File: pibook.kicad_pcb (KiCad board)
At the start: 2 copper layers, 85 x 85 mm, 83 parts, among them IC1 ATTINY48-A, J1 ComputeModule, J2 TRS_JACK_3PIN, P1 CONN_01X40, P2 USB_OTG, P3 CONN_01X02, P4 CONN_02X05, P5 USB_A, P6 CONN_02X06, Q1 Si2323DS, Q2 Si2323DS, Q3 BSS138P, Q4 Si2323DS, SW91 SPST, U1 FAN5333, U2 BQ21040, U3 NCP1532

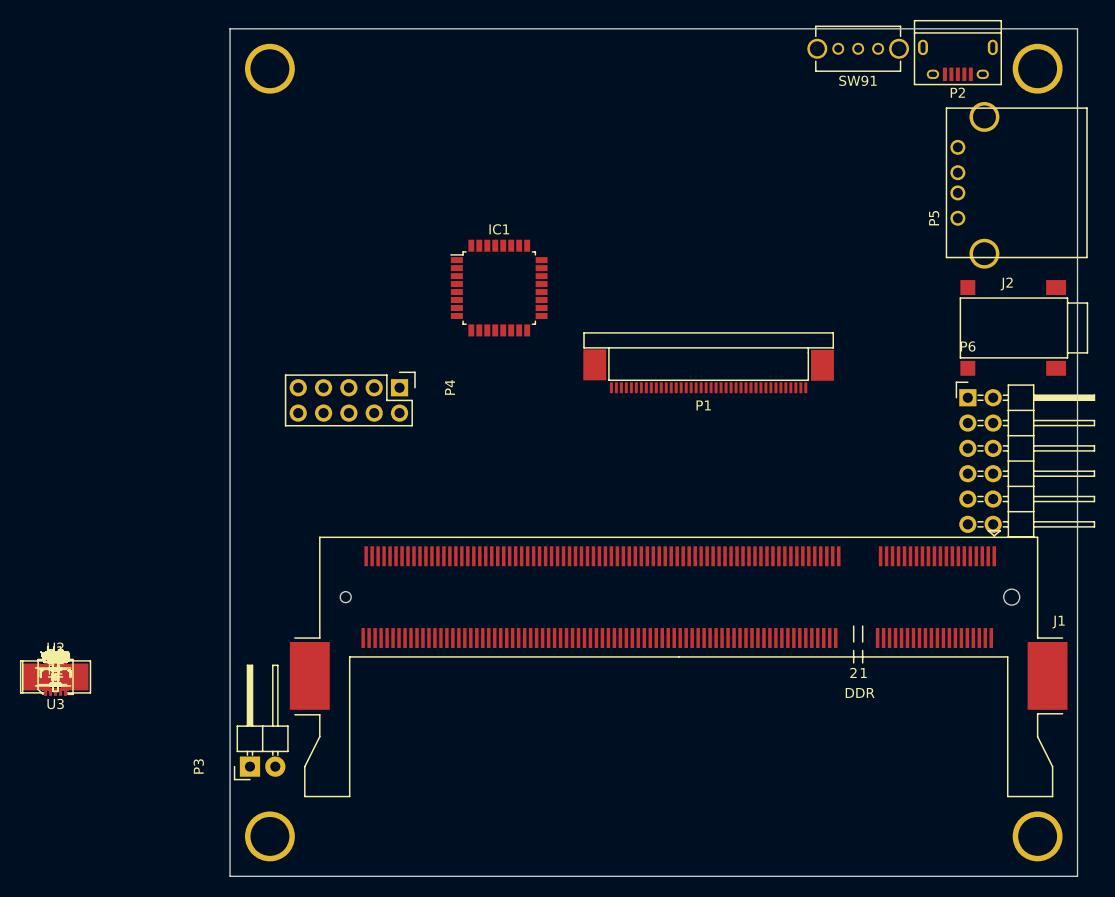
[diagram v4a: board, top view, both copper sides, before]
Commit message: Some more component placement
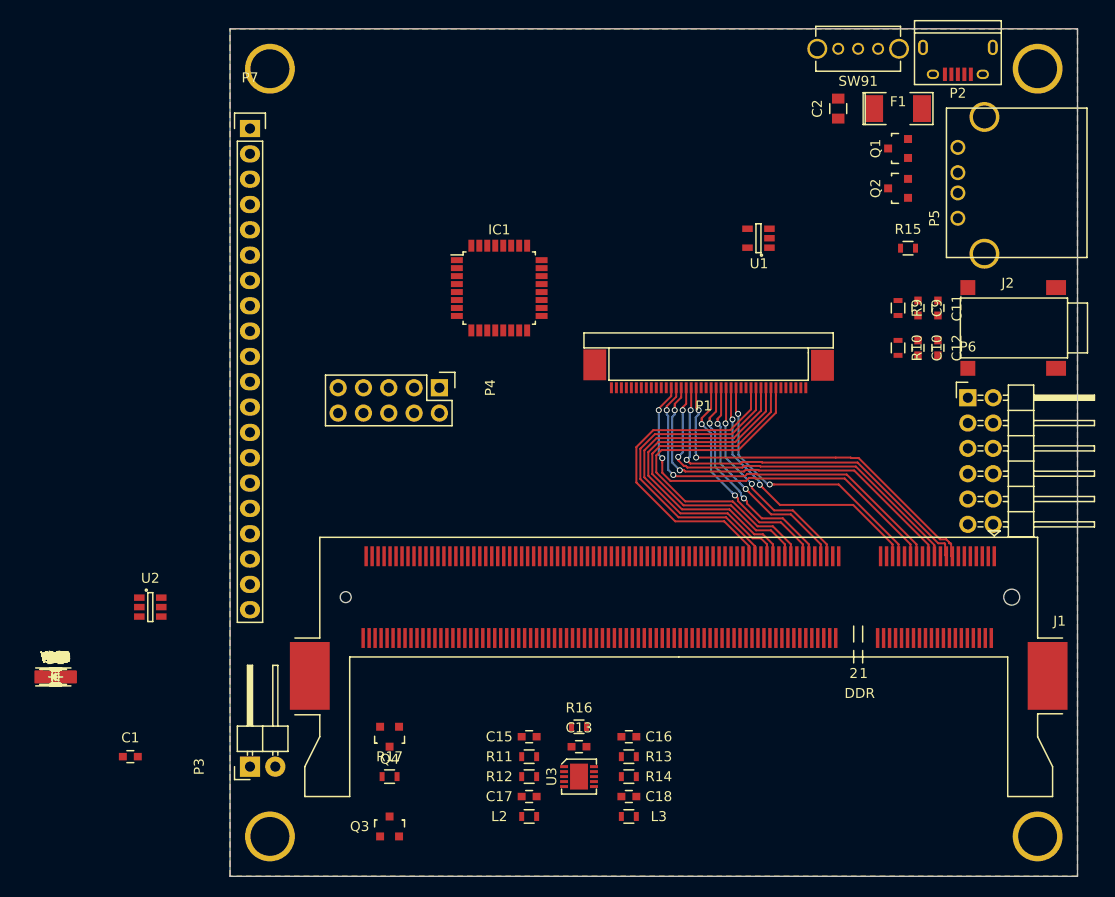
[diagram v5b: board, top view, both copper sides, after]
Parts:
- added P7: CONN_01X20, Pin_Headers:Pin_Header_Straight_1x20, F.Cu at (75.0, 118.0)
- moved F1 101.9 mm to (140.0, 116.0)
- moved Q1 99.7 mm to (140.0, 120.0), turned to 90 degrees
- moved Q2 97.7 mm to (140.0, 124.0), turned to 90 degrees
- moved C2 97.0 mm to (134.0, 116.0), turned to 90 degrees
- moved C11 95.9 mm to (144.0, 136.0), turned to 270 degrees
- moved R15 95.7 mm to (141.0, 130.0)
- moved C12 94.5 mm to (144.0, 140.0), turned to 270 degrees
- moved C9 94.1 mm to (142.0, 136.0), turned to 270 degrees
- moved C10 92.6 mm to (142.0, 140.0), turned to 270 degrees
- moved R9 92.2 mm to (140.0, 136.0), turned to 270 degrees
- moved R10 90.7 mm to (140.0, 140.0), turned to 270 degrees
- moved U1 83.1 mm to (126.0, 129.0), turned to 180 degrees
- moved L3 59.2 mm to (113.0, 187.0)
- moved C18 58.7 mm to (113.0, 185.0), turned to 180 degrees
- moved R14 58.4 mm to (113.0, 183.0)
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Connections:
- IC1 pad 1: (no net) -> /KEY_C3
- IC1 pad 10: (no net) -> /KEY_C6
- IC1 pad 11: (no net) -> /KEY_C7
- IC1 pad 12: (no net) -> /KEY_R1
- IC1 pad 2: (no net) -> /KEY_C4
- IC1 pad 23: (no net) -> /KEY_C8
- IC1 pad 24: (no net) -> /KEY_C9
- IC1 pad 25: (no net) -> /KEY_C10
- IC1 pad 26: (no net) -> /KEY_C11
- IC1 pad 27: (no net) -> /KEY_R0
- IC1 pad 3: (no net) -> /KEY_R4
- IC1 pad 30: (no net) -> /KEY_C0
- IC1 pad 31: (no net) -> /KEY_C1
- IC1 pad 32: (no net) -> /KEY_C2
- IC1 pad 6: (no net) -> /KEY_R5
- IC1 pad 7: (no net) -> /KEY_R2
- IC1 pad 8: (no net) -> /KEY_R3
- IC1 pad 9: (no net) -> /KEY_C5
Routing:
- net /LCD_B_7: track 0.00 -> 38.5 mm, vias 0 -> 2
- net /LCD_B_5: track 0.00 -> 38.3 mm, vias 0 -> 2
- net /LCD_B_3: track 0.00 -> 38.3 mm, vias 0 -> 2
- net /LCD_B_6: track 0.00 -> 38.1 mm, vias 0 -> 2
- net /LCD_B_4: track 0.00 -> 38.1 mm, vias 0 -> 2
- net /LCD_B_2: track 0.00 -> 37.8 mm, vias 0 -> 2
- net /LCD_R_2: track 0.00 -> 35.7 mm
- net /LCD_R_3: track 0.00 -> 35.5 mm
- net /LCD_R_4: track 0.00 -> 34.8 mm
- net /LCD_R_5: track 0.00 -> 34.6 mm
- net /LCD_R_6: track 0.00 -> 33.8 mm
- net /LCD_R_7: track 0.00 -> 33.7 mm
- net /LCD_G_2: track 0.00 -> 28.0 mm, vias 0 -> 2
- net /LCD_G_3: track 0.00 -> 27.9 mm, vias 0 -> 2
- net /LCD_G_7: track 0.00 -> 22.8 mm, vias 0 -> 2
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- added copper zone on B.Cu, net GND
- added copper zone on F.Cu, net GND
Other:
- net class Default: trace_width 0.25 -> 0.2

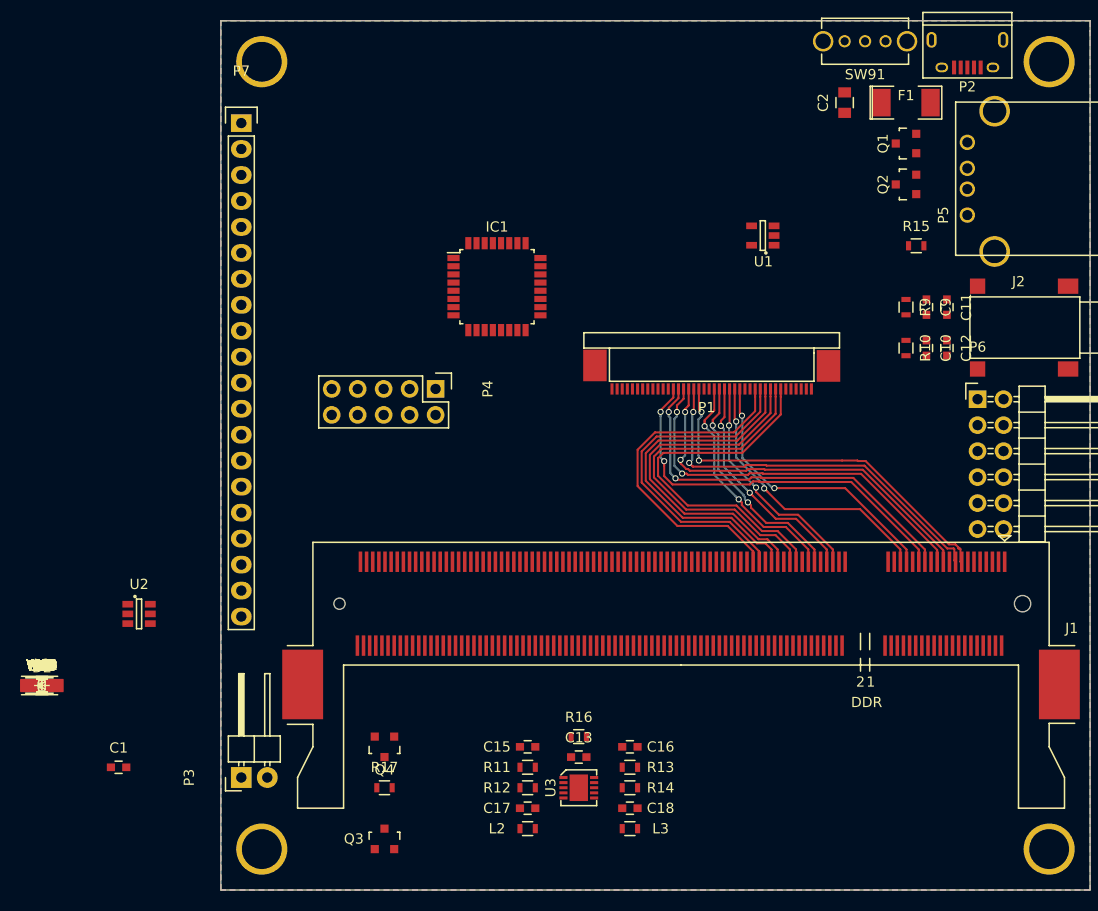
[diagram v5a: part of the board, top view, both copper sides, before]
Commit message: All components placed
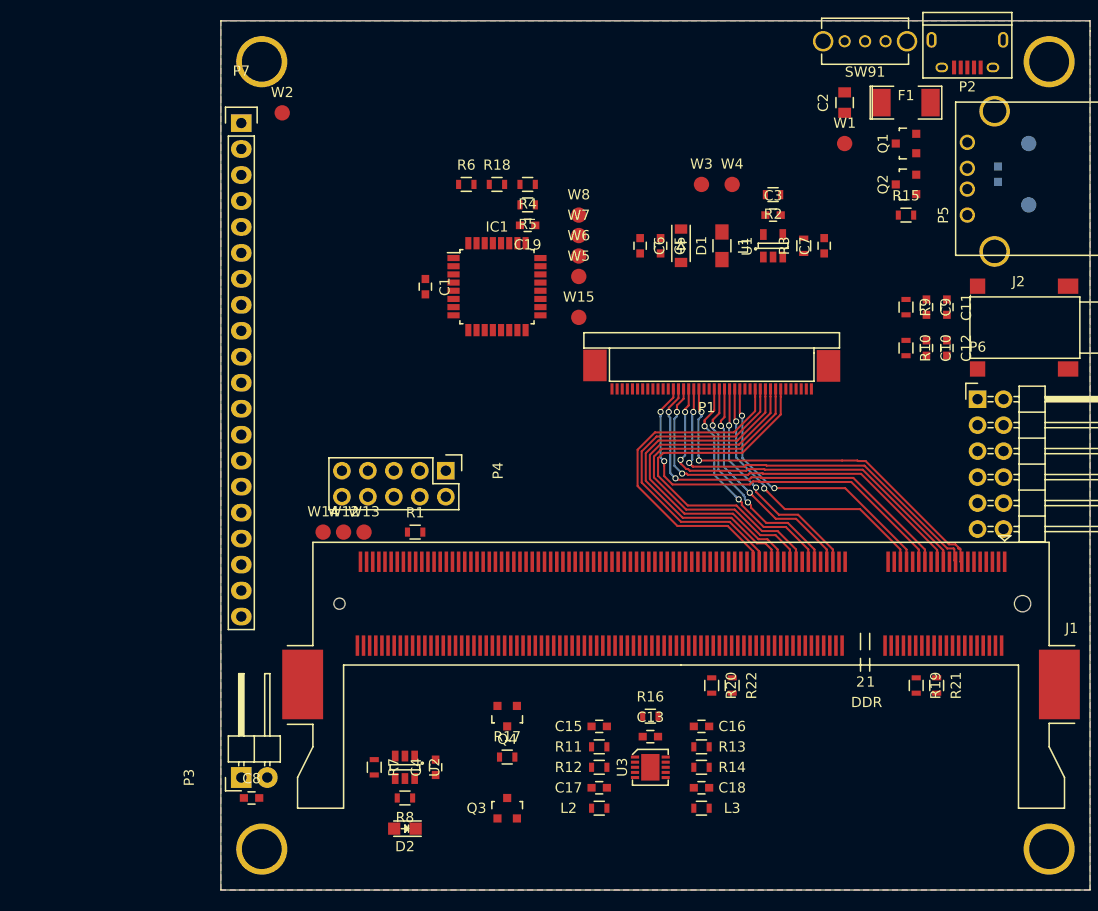
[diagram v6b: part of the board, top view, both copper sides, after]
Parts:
- removed W9: VBAT, Measurement_Points:Measurement_Point_Round-SMD-Pad_Small
- C14, W10, W11: moved to B.Cu
- moved W10 110.1 mm to (152.0, 120.0)
- moved W11 107.3 mm to (152.0, 126.0)
- moved C14 106.0 mm to (149.0, 123.0), turned to 90 degrees
- moved W1 94.7 mm to (134.0, 120.0)
- moved C7 87.8 mm to (132.0, 130.0), turned to 90 degrees
- moved R21 87.5 mm to (143.0, 173.0), turned to 270 degrees
- moved R2 86.1 mm to (127.0, 125.0), turned to 180 degrees
- moved R3 86.0 mm to (130.0, 130.0), turned to 90 degrees
- moved R19 85.5 mm to (141.0, 173.0), turned to 270 degrees
- moved C3 85.0 mm to (127.0, 127.0)
- moved W4 83.4 mm to (123.0, 124.0)
- moved W3 81.0 mm to (120.0, 124.0)
- moved L1 79.2 mm to (122.0, 130.0), turned to 270 degrees
- moved D1 75.9 mm to (118.0, 130.0), turned to 270 degrees
- moved C5 74.2 mm to (116.0, 130.0), turned to 270 degrees
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
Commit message: Some more power routing
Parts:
- added REF**: VIA_0.6MM, ComputeModule:VIA_0.6MM, F.Cu at (96.0, 149.0)
- added REF**: VIA_0.6MM, ComputeModule:VIA_0.6MM, F.Cu at (157.0, 165.0)
- added REF**: VIA_0.6MM, ComputeModule:VIA_0.6MM, F.Cu at (149.0, 183.0)
- added REF**: VIA_0.6MM, ComputeModule:VIA_0.6MM, F.Cu at (143.0, 189.0)
- added REF**: VIA_0.6MM, ComputeModule:VIA_0.6MM, F.Cu at (86.0, 190.0)
- added REF**: VIA_0.6MM, ComputeModule:VIA_0.6MM, F.Cu at (109.0, 190.0)
- added REF**: VIA_0.6MM, ComputeModule:VIA_0.6MM, F.Cu at (74.0, 186.0)
- added REF**: VIA_0.6MM, ComputeModule:VIA_0.6MM, F.Cu at (80.0, 191.0)
- added REF**: VIA_0.6MM, ComputeModule:VIA_0.6MM, F.Cu at (83.0, 184.0)
- added REF**: VIA_0.6MM, ComputeModule:VIA_0.6MM, F.Cu at (90.0, 178.5)
- added REF**: VIA_0.6MM, ComputeModule:VIA_0.6MM, F.Cu at (106.0, 181.0)
- added REF**: VIA_0.6MM, ComputeModule:VIA_0.6MM, F.Cu at (98.0, 151.0)
- added REF** (x2): VIA_0.6MM, ComputeModule:VIA_0.6MM, F.Cu at (92.8, 178.5)
- added REF**: VIA_0.6MM, ComputeModule:VIA_0.6MM, F.Cu at (115.0, 181.0)
- added REF**: VIA_0.6MM, ComputeModule:VIA_0.6MM, F.Cu at (106.0, 175.0)
- added REF**: VIA_0.6MM, ComputeModule:VIA_0.6MM, F.Cu at (115.0, 182.0)
- added REF**: VIA_0.6MM, ComputeModule:VIA_0.6MM, F.Cu at (115.0, 180.0)
- added REF**: VIA_0.6MM, ComputeModule:VIA_0.6MM, F.Cu at (150.0, 191.0)
- added REF**: VIA_0.6MM, ComputeModule:VIA_0.6MM, F.Cu at (156.0, 185.0)
- added REF**: VIA_0.6MM, ComputeModule:VIA_0.6MM, F.Cu at (98.0, 158.0)
- added REF**: VIA_0.6MM, ComputeModule:VIA_0.6MM, F.Cu at (95.0, 158.0)
- added REF**: VIA_0.6MM, ComputeModule:VIA_0.6MM, F.Cu at (157.0, 118.0)
- added REF**: VIA_0.6MM, ComputeModule:VIA_0.6MM, F.Cu at (157.0, 126.0)
- added REF**: VIA_0.6MM, ComputeModule:VIA_0.6MM, F.Cu at (157.0, 136.0)
- added REF**: VIA_0.6MM, ComputeModule:VIA_0.6MM, F.Cu at (157.0, 144.0)
- added REF**: VIA_0.6MM, ComputeModule:VIA_0.6MM, F.Cu at (157.0, 154.0)
- C14: moved to F.Cu
- moved R16 18.4 mm to (101.0, 188.0)
- moved C1 8.66 mm to (99.2, 140.0), turned to 0 degrees
- moved C14 7.00 mm to (142.0, 123.0)
- moved C13 6.00 mm to (115.0, 184.0)
- moved Q1 2.24 mm to (139.0, 122.0)
- moved R15 2.24 mm to (142.0, 126.0), turned to 90 degrees
- moved C3 2.00 mm to (127.0, 129.0)
- moved C5 2.00 mm to (116.0, 132.0)
- moved C6 2.00 mm to (114.0, 132.0)
- moved C7 2.00 mm to (132.0, 132.0)
- moved D1 2.00 mm to (118.0, 132.0)
- moved L1 2.00 mm to (122.0, 132.0)
- moved R2 2.00 mm to (127.0, 127.0)
- moved R3 2.00 mm to (130.0, 132.0)
- moved U1 2.00 mm to (127.0, 132.0)
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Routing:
- net +BATT: track 0.00 -> 271.4 mm, vias 0 -> 5
- net /PWR_ENABLE: track 0.00 -> 168.5 mm, vias 0 -> 3
- net +VUSB_IN: track 0.00 -> 154.6 mm
- net /USB_D-: track 0.00 -> 82.0 mm
- net /USB_D+: track 0.00 -> 80.9 mm
- net +1V8: track 0.00 -> 59.9 mm
- net +3V3: track 0.00 -> 59.8 mm
- net /LCD_CLK: track 0.00 -> 46.8 mm, vias 0 -> 2
- net /LCD_DEN: track 0.00 -> 46.8 mm, vias 0 -> 2
- net /LCD_VSYNC: track 0.00 -> 42.9 mm, vias 0 -> 2
- net /LCD_HSYNC: track 0.00 -> 41.6 mm, vias 0 -> 2
- net /CM_VBAT: track 0.00 -> 33.7 mm
- net Net-(R8-Pad2): track 0.00 -> 18.0 mm
- net Net-(C16-Pad2): track 0.00 -> 8.20 mm
- net Net-(C15-Pad2): track 0.00 -> 8.20 mm
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
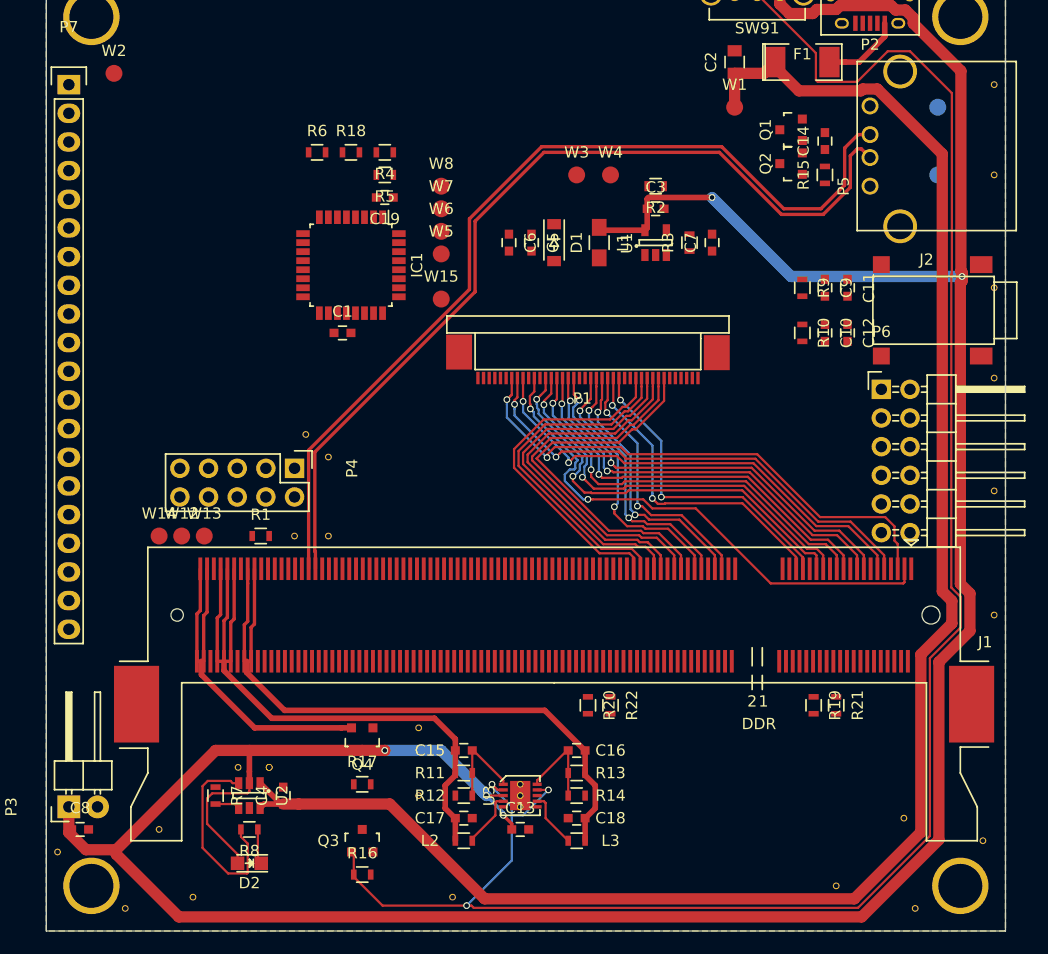
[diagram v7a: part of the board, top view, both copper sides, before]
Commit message: AVR route out mostly done
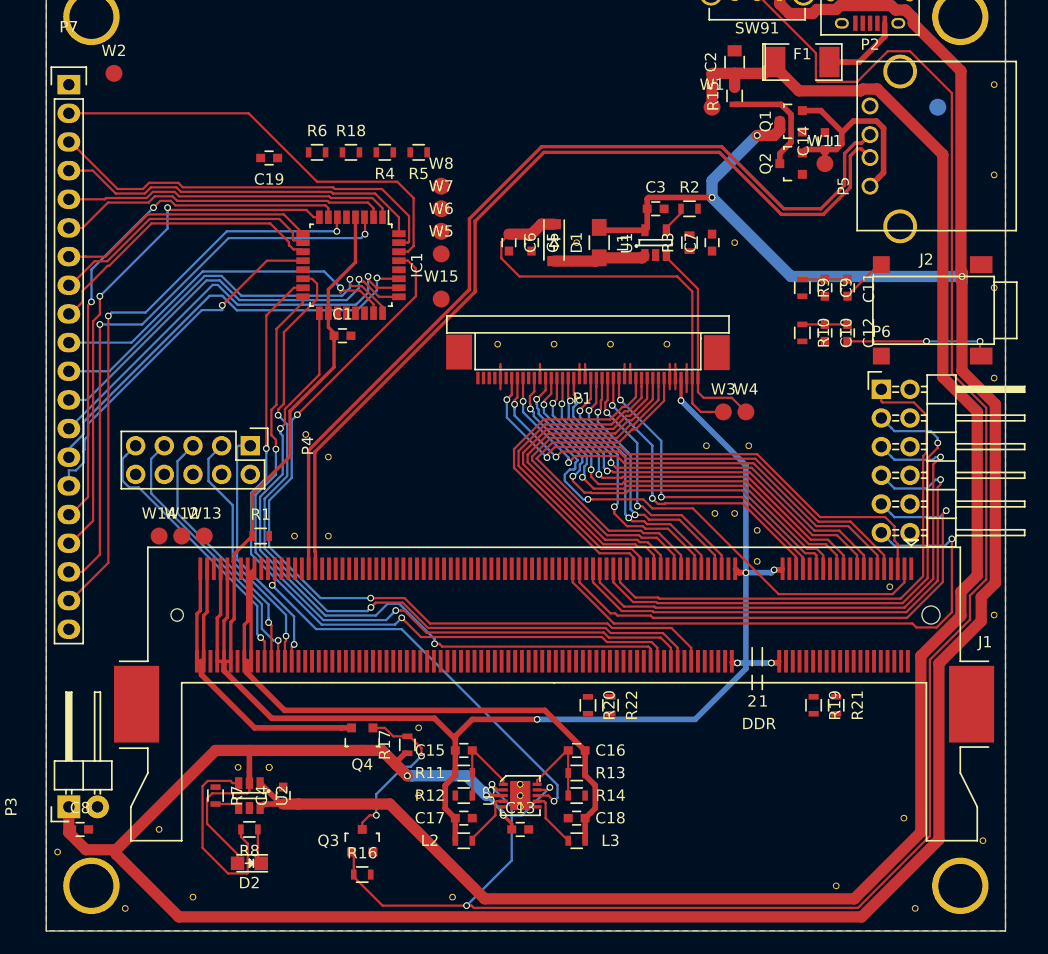
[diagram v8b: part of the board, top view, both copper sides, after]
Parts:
- removed the REF** at (157.0, 154.0)
- added REF**: VIA_0.6MM, ComputeModule:VIA_0.6MM, F.Cu at (136.0, 157.5)
- added REF**: VIA_0.6MM, ComputeModule:VIA_0.6MM, F.Cu at (120.0, 132.0)
- added REF**: VIA_0.6MM, ComputeModule:VIA_0.6MM, F.Cu at (136.0, 160.2)
- added REF**: VIA_0.6MM, ComputeModule:VIA_0.6MM, F.Cu at (132.2, 156.0)
- added REF**: VIA_0.6MM, ComputeModule:VIA_0.6MM, F.Cu at (147.8, 162.5)
- added REF**: VIA_0.6MM, ComputeModule:VIA_0.6MM, F.Cu at (134.0, 156.0)
- added REF**: VIA_0.6MM, ComputeModule:VIA_0.6MM, F.Cu at (135.2, 150.0)
- added REF**: VIA_0.6MM, ComputeModule:VIA_0.6MM, F.Cu at (131.5, 150.0)
- added REF**: VIA_0.6MM, ComputeModule:VIA_0.6MM, F.Cu at (128.0, 141.0)
- added REF**: VIA_0.6MM, ComputeModule:VIA_0.6MM, F.Cu at (123.0, 141.0)
- added REF**: VIA_0.6MM, ComputeModule:VIA_0.6MM, F.Cu at (118.0, 141.0)
- added REF**: VIA_0.6MM, ComputeModule:VIA_0.6MM, F.Cu at (113.0, 141.0)
- added REF**: VIA_0.6MM, ComputeModule:VIA_0.6MM, F.Cu at (134.0, 132.0)
- W11: moved to F.Cu
- moved W3 24.7 mm to (133.0, 147.0)
- moved W4 24.2 mm to (135.0, 147.0)
- moved C19 10.8 mm to (92.8, 124.5)
- moved R15 10.6 mm to (134.0, 119.0)
- moved W11 10.0 mm to (142.0, 125.0)
- moved R17 5.32 mm to (105.0, 176.5), turned to 90 degrees
- moved P4 4.40 mm to (91.1, 150.0)
- moved R2 3.61 mm to (130.0, 129.0), turned to 0 degrees
- moved R5 3.61 mm to (106.0, 124.0)
- moved W1 2.00 mm to (132.0, 120.0)
- moved Q1 0.75 mm to (139.0, 121.2)
- moved C1 0.25 mm to (99.2, 140.2)
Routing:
- net +3V3: track 59.8 -> 161.1 mm, vias 0 -> 6
- net /AVR_~RST: track 0.00 -> 74.1 mm, vias 0 -> 2
- net /AVR_~CS: track 0.00 -> 69.5 mm, vias 0 -> 2
- net /AVR_MOSI: track 0.00 -> 67.1 mm, vias 0 -> 2
- net /AVR_MISO: track 0.00 -> 66.9 mm, vias 0 -> 2
- net /AVR_SCK: track 0.00 -> 63.8 mm, vias 0 -> 2
- net /KEY_R4: track 0.00 -> 52.1 mm, vias 0 -> 2
- net /KEY_R5: track 0.00 -> 51.4 mm, vias 0 -> 2
- net /USER_IO_5: track 0.00 -> 50.5 mm, vias 0 -> 1
- net /USER_IO_2: track 0.00 -> 49.6 mm, vias 0 -> 1
- net /USER_IO_0: track 0.00 -> 49.5 mm
- net /USER_IO_1: track 0.00 -> 49.3 mm, vias 0 -> 1
- net /USER_IO_3: track 0.00 -> 49.1 mm, vias 0 -> 1
- net /USER_IO_4: track 0.00 -> 48.9 mm, vias 0 -> 1
- net /KEY_R3: track 0.00 -> 47.3 mm, vias 0 -> 2
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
